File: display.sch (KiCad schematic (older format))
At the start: 4 parts, among them U6 LS013B4DN04

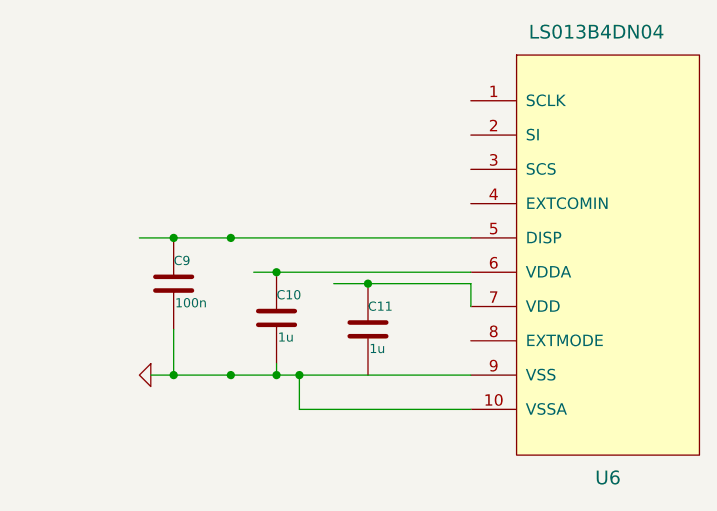
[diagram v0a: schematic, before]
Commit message: Add gps
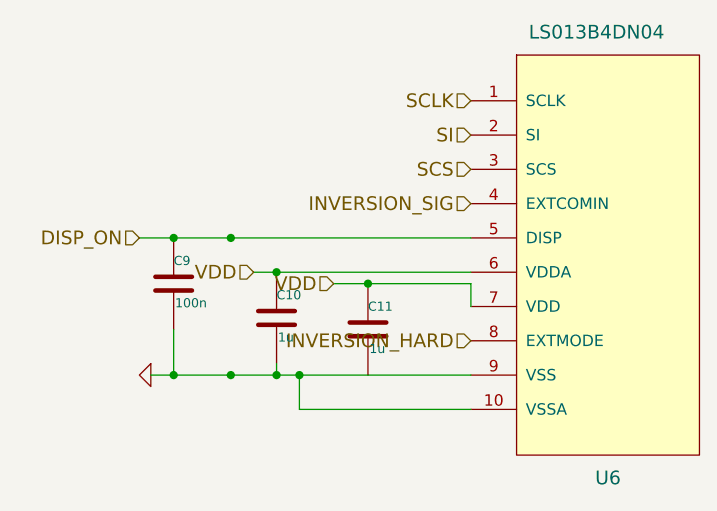
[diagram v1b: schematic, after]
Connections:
- net labels added: DISP_ON, INVERSION_HARD, INVERSION_SIG, SCLK, SCS, SI, VDD
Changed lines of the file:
@@
 $Descr A4 11693 8268
 encoding utf-8
-Sheet 7 10
+Sheet 7 11
 Title ""
 Date ""
@@
 $EndComp
 $Comp
-L GND #PWR11
+L GND #PWR17
 U 1 1 54463B98
 P 3950 3900
-F 0 "#PWR11" H 3950 3900 30  0001 C CNN
+F 0 "#PWR17" H 3950 3900 30  0001 C CNN
 F 1 "GND" H 3950 3830 30  0001 C CNN
 F 2 "" H 3950 3900 60  0000 C CNN
@@
 Connection ~ 4900 3500
 Connection ~ 4050 3300
+Text HLabel 5350 2700 0    60   Input ~ 0
+SCLK
+Text HLabel 5350 2850 0    60   Input ~ 0
+SI
+Text HLabel 5350 3000 0    60   Input ~ 0
+SCS
+Text HLabel 3900 3300 0    60   Input ~ 0
+DISP_ON
+Text HLabel 4400 3450 0    60   Input ~ 0
+VDD
+Text HLabel 4750 3500 0    60   Input ~ 0
+VDD
+Text HLabel 5350 3150 0    60   Input ~ 0
+INVERSION_SIG
+Text HLabel 5350 3750 0    60   Input ~ 0
+INVERSION_HARD
 $EndSCHEMATC

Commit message: More connections
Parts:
- C10, C11: footprint (none) -> buq2:SM0805
- C9: footprint (none) -> buq2:SM0603
- U6: footprint (none) -> buq2:FPC-CONN-10-FCI-BOTTOM-CONTACTS
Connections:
- net INVERSION_HARD renamed INVERSION_PROG
- net SCS renamed CS
- net SI renamed MOSI
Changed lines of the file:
@@
 F 0 "U6" H 5950 2050 60  0000 C CNN
 F 1 "LS013B4DN04" H 5900 4000 60  0000 C CNN
-F 2 "" H 5600 3200 60  0001 C CNN
+F 2 "buq2:FPC-CONN-10-FCI-BOTTOM-CONTACTS" H 5600 3200 60  0001 C CNN
 F 3 "" H 5600 3200 60  0000 C CNN
 	1    5600 3200
@@
 $EndComp
 $Comp
-L GND #PWR17
+L GND #PWR019
 U 1 1 54463B98
 P 3950 3900
-F 0 "#PWR17" H 3950 3900 30  0001 C CNN
+F 0 "#PWR019" H 3950 3900 30  0001 C CNN
 F 1 "GND" H 3950 3830 30  0001 C CNN
 F 2 "" H 3950 3900 60  0000 C CNN
@@
 F 0 "C9" H 4050 3600 40  0000 L CNN
 F 1 "100n" H 4056 3415 40  0000 L CNN
-F 2 "" H 4088 3350 30  0001 C CNN
+F 2 "buq2:SM0603" H 4088 3350 30  0001 C CNN
 F 3 "" H 4050 3500 60  0000 C CNN
 	1    4050 3500
@@
 F 0 "C10" H 4500 3750 40  0000 L CNN
 F 1 "1u" H 4506 3565 40  0000 L CNN
-F 2 "" H 4538 3500 30  0001 C CNN
+F 2 "buq2:SM0805" H 4538 3500 30  0001 C CNN
 F 3 "" H 4500 3650 60  0000 C CNN
 	1    4500 3650
@@
 F 0 "C11" H 4900 3800 40  0000 L CNN
 F 1 "1u" H 4906 3615 40  0000 L CNN
-F 2 "" H 4938 3550 30  0001 C CNN
+F 2 "buq2:SM0805" H 4938 3550 30  0001 C CNN
 F 3 "" H 4900 3700 60  0000 C CNN
 	1    4900 3700
@@
 SCLK
 Text HLabel 5350 2850 0    60   Input ~ 0
-SI
+MOSI
 Text HLabel 5350 3000 0    60   Input ~ 0
-SCS
+CS
 Text HLabel 3900 3300 0    60   Input ~ 0
 DISP_ON
@@
 INVERSION_SIG
 Text HLabel 5350 3750 0    60   Input ~ 0
-INVERSION_HARD
+INVERSION_PROG
 $EndSCHEMATC

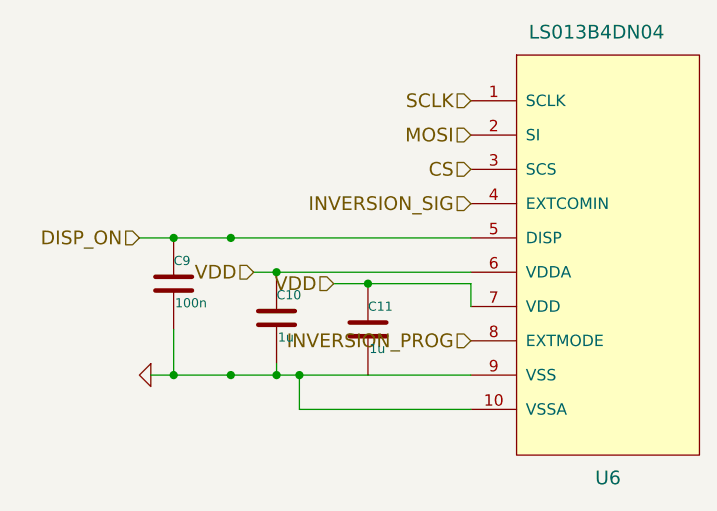
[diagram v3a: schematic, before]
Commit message: Add flash and ram. Some connections and DRC cleaning
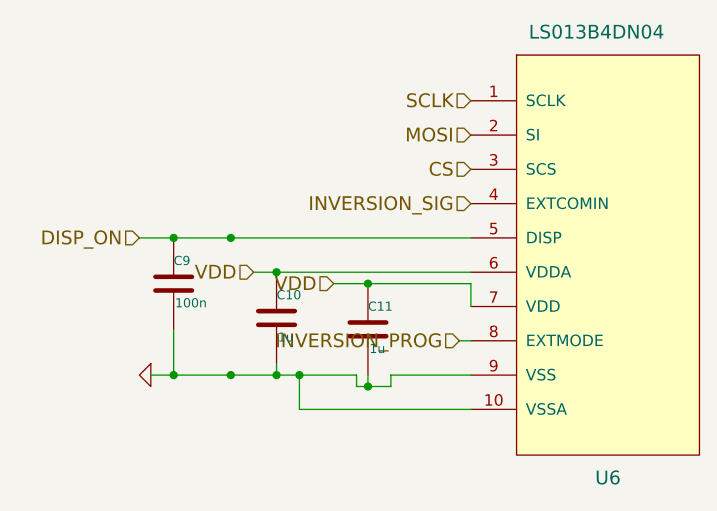
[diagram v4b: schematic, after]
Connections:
- net GND: now also C11.2
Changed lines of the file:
@@
 $Descr A4 11693 8268
 encoding utf-8
-Sheet 7 12
+Sheet 7 13
 Title ""
 Date ""
@@
 $EndComp
 $Comp
-L GND #PWR019
+L GND #PWR020
 U 1 1 54463B98
 P 3950 3900
-F 0 "#PWR019" H 3950 3900 30  0001 C CNN
+F 0 "#PWR020" H 3950 3900 30  0001 C CNN
 F 1 "GND" H 3950 3830 30  0001 C CNN
 F 2 "" H 3950 3900 60  0000 C CNN
@@
 	1    0    0    -1
 $EndComp
-Wire Wire Line
-	3950 3900 5350 3900
 Wire Wire Line
 	4600 4050 5350 4050
@@
 Text HLabel 5350 3150 0    60   Input ~ 0
 INVERSION_SIG
-Text HLabel 5350 3750 0    60   Input ~ 0
+Text HLabel 5300 3750 0    60   Input ~ 0
 INVERSION_PROG
+Wire Wire Line
+	5350 3900 5000 3900
+Wire Wire Line
+	5000 3900 5000 3950
+Wire Wire Line
+	5000 3950 4850 3950
+Wire Wire Line
+	4850 3950 4850 3900
+Wire Wire Line
+	4850 3900 3950 3900
+Wire Wire Line
+	4900 3900 4900 3950
+Connection ~ 4900 3950
+Wire Wire Line
+	5300 3750 5350 3750
 $EndSCHEMATC

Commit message: Add buttons. Fix DRC. Add antenna
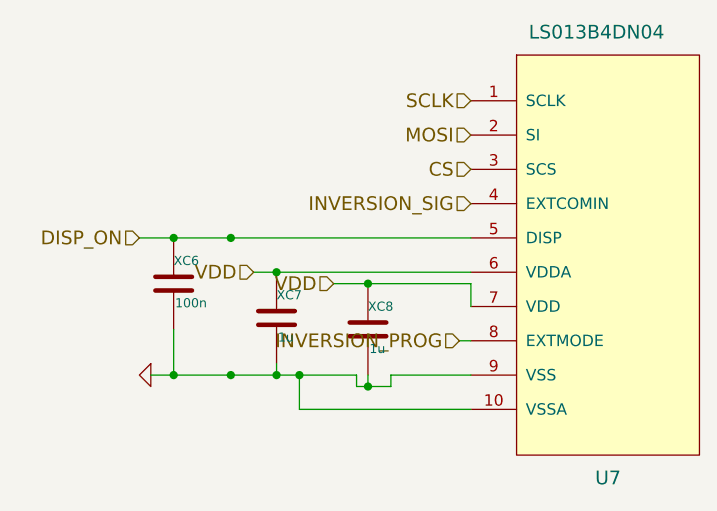
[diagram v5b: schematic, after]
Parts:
- renumbered U6 to U7, C9 to XC6, C10 to XC7, C11 to XC8
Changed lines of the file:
@@
 $Descr A4 11693 8268
 encoding utf-8
-Sheet 7 13
+Sheet 7 14
 Title ""
 Date ""
@@
 $EndDescr
 $Comp
-L LS013B4DN04 U6
+L LS013B4DN04 U7
 U 1 1 54463B91
 P 5600 3200
-F 0 "U6" H 5950 2050 60  0000 C CNN
+F 0 "U7" H 5950 2050 60  0000 C CNN
 F 1 "LS013B4DN04" H 5900 4000 60  0000 C CNN
 F 2 "buq2:FPC-CONN-10-FCI-BOTTOM-CONTACTS" H 5600 3200 60  0001 C CNN
@@
 $EndComp
 $Comp
-L GND #PWR020
+L GND #PWR023
 U 1 1 54463B98
 P 3950 3900
-F 0 "#PWR020" H 3950 3900 30  0001 C CNN
+F 0 "#PWR023" H 3950 3900 30  0001 C CNN
 F 1 "GND" H 3950 3830 30  0001 C CNN
 F 2 "" H 3950 3900 60  0000 C CNN
@@
 $EndComp
 $Comp
-L C C9
+L C XC6
 U 1 1 54463B9E
 P 4050 3500
-F 0 "C9" H 4050 3600 40  0000 L CNN
+F 0 "XC6" H 4050 3600 40  0000 L CNN
 F 1 "100n" H 4056 3415 40  0000 L CNN
 F 2 "buq2:SM0603" H 4088 3350 30  0001 C CNN
@@
 Connection ~ 4300 3900
 $Comp
-L C C10
+L C XC7
 U 1 1 54463BAA
 P 4500 3650
-F 0 "C10" H 4500 3750 40  0000 L CNN
+F 0 "XC7" H 4500 3750 40  0000 L CNN
 F 1 "1u" H 4506 3565 40  0000 L CNN
 F 2 "buq2:SM0805" H 4538 3500 30  0001 C CNN
@@
 Connection ~ 4500 3900
 $Comp
-L C C11
+L C XC8
 U 1 1 54463BB4
 P 4900 3700
-F 0 "C11" H 4900 3800 40  0000 L CNN
+F 0 "XC8" H 4900 3800 40  0000 L CNN
 F 1 "1u" H 4906 3615 40  0000 L CNN
 F 2 "buq2:SM0805" H 4938 3550 30  0001 C CNN

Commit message: Start first layout test
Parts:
- XC7, XC8: footprint buq2:SM0805 -> buq2:SM0603
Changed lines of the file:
@@
 F 0 "XC7" H 4500 3750 40  0000 L CNN
 F 1 "1u" H 4506 3565 40  0000 L CNN
-F 2 "buq2:SM0805" H 4538 3500 30  0001 C CNN
+F 2 "buq2:SM0603" H 4538 3500 30  0001 C CNN
 F 3 "" H 4500 3650 60  0000 C CNN
 	1    4500 3650
@@
 F 0 "XC8" H 4900 3800 40  0000 L CNN
 F 1 "1u" H 4906 3615 40  0000 L CNN
-F 2 "buq2:SM0805" H 4938 3550 30  0001 C CNN
+F 2 "buq2:SM0603" H 4938 3550 30  0001 C CNN
 F 3 "" H 4900 3700 60  0000 C CNN
 	1    4900 3700

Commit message: Start planning test board v2.0
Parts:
- U7: footprint buq2:FPC-CONN-10-FCI-BOTTOM-CONTACTS -> buq2:FPC-CONN-10-FCI-TOP-CONTACTS
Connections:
- net INVERSION_PROG is gone; now on net GND: U7.8 (EXTMODE)
- net INVERSION_SIG is gone; now on net GND: U7.4 (EXTCOMIN)
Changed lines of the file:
@@
 $Descr A4 11693 8268
 encoding utf-8
-Sheet 7 14
+Sheet 6 10
 Title ""
 Date ""
@@
 F 0 "U7" H 5950 2050 60  0000 C CNN
 F 1 "LS013B4DN04" H 5900 4000 60  0000 C CNN
-F 2 "buq2:FPC-CONN-10-FCI-BOTTOM-CONTACTS" H 5600 3200 60  0001 C CNN
+F 2 "buq2:FPC-CONN-10-FCI-TOP-CONTACTS" H 5600 3200 60  0001 C CNN
 F 3 "" H 5600 3200 60  0000 C CNN
 	1    5600 3200
@@
 $EndComp
 $Comp
-L GND #PWR023
+L GND #PWR021
 U 1 1 54463B98
 P 3950 3900
-F 0 "#PWR023" H 3950 3900 30  0001 C CNN
+F 0 "#PWR021" H 3950 3900 30  0001 C CNN
 F 1 "GND" H 3950 3830 30  0001 C CNN
 F 2 "" H 3950 3900 60  0000 C CNN
@@
 Text HLabel 4750 3500 0    60   Input ~ 0
 VDD
-Text HLabel 5350 3150 0    60   Input ~ 0
-INVERSION_SIG
-Text HLabel 5300 3750 0    60   Input ~ 0
-INVERSION_PROG
 Wire Wire Line
 	5350 3900 5000 3900
@@
 Connection ~ 4900 3950
 Wire Wire Line
-	5300 3750 5350 3750
+	5200 3750 5350 3750
+$Comp
+L GND #PWR022
+U 1 1 54C7430F
+P 5100 3150
+F 0 "#PWR022" H 5100 3150 30  0001 C CNN
+F 1 "GND" H 5100 3080 30  0001 C CNN
+F 2 "" H 5100 3150 60  0000 C CNN
+F 3 "" H 5100 3150 60  0000 C CNN
+	1    5100 3150
+	0    1    1    0
+$EndComp
+Wire Wire Line
+	5100 3150 5350 3150
+$Comp
+L GND #PWR023
+U 1 1 54C74349
+P 5200 3750
+F 0 "#PWR023" H 5200 3750 30  0001 C CNN
+F 1 "GND" H 5200 3680 30  0001 C CNN
+F 2 "" H 5200 3750 60  0000 C CNN
+F 3 "" H 5200 3750 60  0000 C CNN
+	1    5200 3750
+	0    1    1    0
+$EndComp
 $EndSCHEMATC
